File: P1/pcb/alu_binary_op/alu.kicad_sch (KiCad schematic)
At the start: 23 parts, among them J1 650473-5, U13 74LS541, U14 74HC86, U15 74HC86, U16 74LS621, U17 74LS08, U18 74LS08, U19 74LS621, U20 74LS32, U21 74LS32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

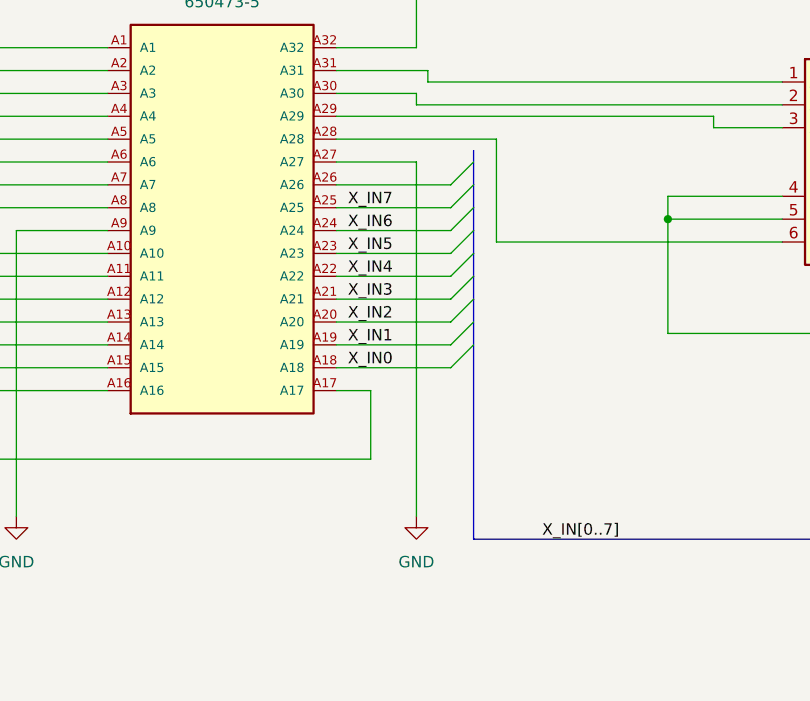
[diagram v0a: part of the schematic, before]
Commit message: Removed unneeded backup files
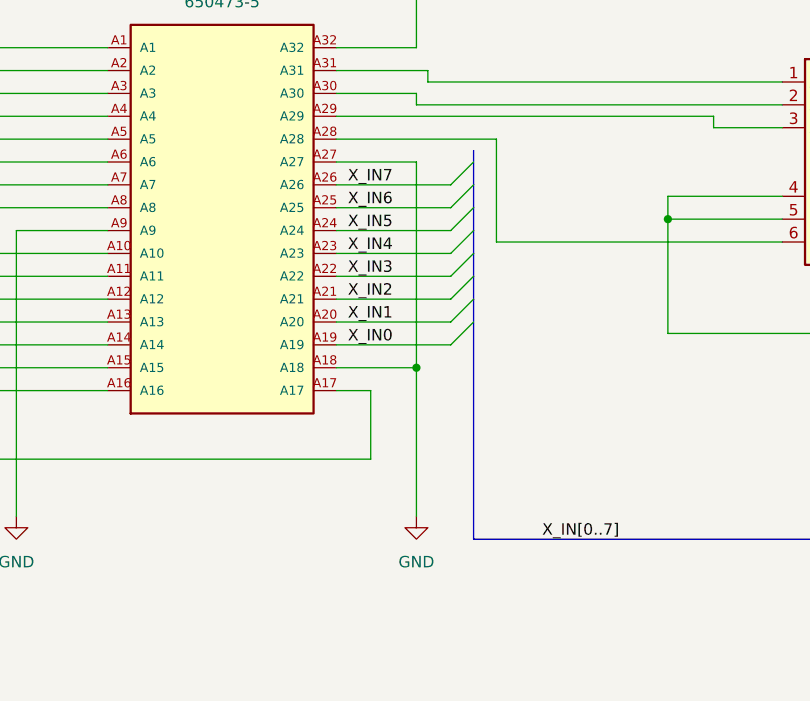
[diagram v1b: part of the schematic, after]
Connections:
- net GND: now also J1.A18
- net X_IN0: now also J1.A19; no longer J1.A18
- net X_IN1: now also J1.A20; no longer J1.A19
- net X_IN2: now also J1.A21; no longer J1.A20
- net X_IN3: now also J1.A22; no longer J1.A21
- net X_IN4: now also J1.A23; no longer J1.A22
- net X_IN5: now also J1.A24; no longer J1.A23
- net X_IN6: now also J1.A25; no longer J1.A24
- net X_IN7: now also J1.A26; no longer J1.A25
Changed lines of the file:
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@@
 	)
 	(junction
+		(at 119.38 73.66)
+		(diameter 0)
+		(color 0 0 0 0)
+	)
+	(junction
 		(at 49.53 400.05)
 		(diameter 0)
@@
 	)
 	(bus_entry
-		(at 123.19 73.66)
-		(size 2.54 -2.54)
-		(stroke
-			(width 0)
-			(type default)
-		)
-	)
-	(bus_entry
 		(at 121.92 472.44)
 		(size 2.54 2.54)
@@
 		)
 	)
+	(wire
+		(pts
+			(xy 110.49 73.66) (xy 119.38 73.66)
+		)
+		(stroke
+			(width 0)
+			(type default)
+		)
+	)
 	(bus
 		(pts
@@
 		)
 	)
+	(wire
+		(pts
+			(xy 119.38 73.66) (xy 119.38 90.17)
+		)
+		(stroke
+			(width 0)
+			(type default)
+		)
+	)
 	(bus
 		(pts
@@
 		)
 	)
-	(bus
-		(pts
-			(xy 125.73 68.58) (xy 125.73 71.12)
-		)
-		(stroke
-			(width 0)
-			(type default)
-		)
-	)
 	(wire
 		(pts
@@
 	(wire
 		(pts
-			(xy 110.49 73.66) (xy 123.19 73.66)
-		)
-		(stroke
-			(width 0)
-			(type default)
-		)
-	)
-	(wire
-		(pts
 			(xy 1115.06 49.53) (xy 1120.14 49.53)
 		)
@@
 	(wire
 		(pts
-			(xy 119.38 50.8) (xy 119.38 90.17)
+			(xy 119.38 50.8) (xy 119.38 73.66)
 		)
 		(stroke
@@
 	(bus
 		(pts
-			(xy 125.73 71.12) (xy 125.73 92.71)
+			(xy 125.73 68.58) (xy 125.73 92.71)
 		)
 		(stroke
@@
 		)
 	)
-	(label "X_IN6"
-		(at 111.76 58.42 0)
+	(label "X_IN3"
+		(at 111.76 63.5 0)
 		(fields_autoplaced yes)
 		(effects
@@
 		)
 	)
-	(label "X_IN7"
-		(at 111.76 55.88 0)
-		(fields_autoplaced yes)
-		(effects
-			(font
-				(size 1.27 1.27)
-			)
-			(justify left bottom)
-		)
-	)
 	(label "X_IN5"
 		(at 345.44 227.33 0)
@@
 		)
 	)
-	(label "X_IN0"
-		(at 111.76 73.66 0)
+	(label "Y_OUT0"
+		(at 151.13 314.96 0)
 		(fields_autoplaced yes)
 		(effects
@@
 		)
 	)
-	(label "Y_OUT0"
-		(at 151.13 314.96 0)
+	(label "Y_OUT7"
+		(at 153.67 558.8 0)
 		(fields_autoplaced yes)
 		(effects
@@
 		)
 	)
-	(label "Y_OUT7"
-		(at 153.67 558.8 0)
+	(label "Y_OUT5"
+		(at 152.4 514.35 0)
 		(fields_autoplaced yes)
 		(effects
@@
 		)
 	)
-	(label "Y_OUT5"
-		(at 152.4 514.35 0)
+	(label "X_IN5"
+		(at 111.76 58.42 0)
 		(fields_autoplaced yes)
 		(effects
@@
 		)
 	)
+	(label "X_IN0"
+		(at 111.76 71.12 0)
+		(fields_autoplaced yes)
+		(effects
+			(font
+				(size 1.27 1.27)
+			)
+			(justify left bottom)
+		)
+	)
 	(label "Y_OUT5"
 		(at 147.32 220.98 0)
@@
 		)
 	)
-	(label "X_OUT3"
-		(at 128.27 199.39 0)
+	(label "X_IN7"
+		(at 111.76 53.34 0)
 		(fields_autoplaced yes)
 		(effects
@@
 		)
 	)
-	(label "Y_OUT5"
-		(at 44.45 73.66 0)
+	(label "X_OUT3"
+		(at 128.27 199.39 0)
 		(fields_autoplaced yes)
 		(effects
@@
 		)
 	)
-	(label "Y_OUT3"
-		(at 152.4 344.17 0)
+	(label "Y_OUT5"
+		(at 44.45 73.66 0)
 		(fields_autoplaced yes)
 		(effects
@@
 		)
 	)
-	(label "Y_OUT6"
-		(at 147.32 252.73 0)
+	(label "Y_OUT3"
+		(at 152.4 344.17 0)
 		(fields_autoplaced yes)
 		(effects
@@
 		)
 	)
-	(label "X_IN5"
-		(at 111.76 60.96 0)
+	(label "Y_OUT6"
+		(at 147.32 252.73 0)
 		(fields_autoplaced yes)
 		(effects
@@
 		)
 	)
-	(label "X_IN4"
-		(at 111.76 63.5 0)
-		(fields_autoplaced yes)
-		(effects
-			(font
-				(size 1.27 1.27)
-			)
-			(justify left bottom)
-		)
-	)
 	(label "Y_OUT2"
 		(at 44.45 66.04 0)
@@
 		)
 	)
-	(label "X_IN3"
-		(at 111.76 66.04 0)
-		(fields_autoplaced yes)
-		(effects
-			(font
-				(size 1.27 1.27)
-			)
-			(justify left bottom)
-		)
-	)
 	(label "X_OUT7"
 		(at 128.27 408.94 0)
@@
 		)
 	)
-	(label "X_IN1"
-		(at 111.76 71.12 0)
-		(fields_autoplaced yes)
-		(effects
-			(font
-				(size 1.27 1.27)
-			)
-			(justify left bottom)
-		)
-	)
 	(label "Y_OUT4"
 		(at 152.4 528.32 0)
@@
 		)
 	)
-	(label "X_OUT0"
-		(at 128.27 320.04 0)
+	(label "X_IN2"
+		(at 111.76 66.04 0)
 		(fields_autoplaced yes)
 		(effects
@@
 		)
 	)
-	(label "X_IN2"
-		(at 111.76 68.58 0)
+	(label "X_OUT0"
+		(at 128.27 320.04 0)
 		(fields_autoplaced yes)
 		(effects
@@
 		)
 	)
+	(label "X_IN4"
+		(at 111.76 60.96 0)
+		(fields_autoplaced yes)
+		(effects
+			(font
+				(size 1.27 1.27)
+			)
+			(justify left bottom)
+		)
+	)
 	(label "X_IN3"
 		(at 345.44 217.17 0)
@@
 		)
 	)
+	(label "X_IN6"
+		(at 111.76 55.88 0)
+		(fields_autoplaced yes)
+		(effects
+			(font
+				(size 1.27 1.27)
+			)
+			(justify left bottom)
+		)
+	)
 	(label "X_IN4"
 		(at 345.44 361.95 0)
@@
 		(fields_autoplaced yes)
 		(effects
+			(font
+				(size 1.27 1.27)
+			)
+			(justify left bottom)
+		)
+	)
+	(label "X_IN1"
+		(at 111.76 68.58 0)
+		(fields_autoplaced yes)
+		(effects
